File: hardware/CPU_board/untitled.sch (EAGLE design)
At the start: 67 parts, among them IC1 MAX232ECWE, IC2 MAX232ECWE, IC3 AM29F040J, IC4 74HCT138D, IC5 LM2596S, IC6 74245SSOP, IC7 74245SSOP, IC8 74245SSOP, J2 POWER_JACKSLT, U1 AS6C4008-55SIN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

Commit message: Power trace updated
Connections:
- net 5V: now also IC7P.VCC, IC8P.VCC
- net GND: now also IC7P.GND, IC8A.A1, IC8A.A2, IC8A.A3, IC8A.A4, IC8A.G, IC8P.GND
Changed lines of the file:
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@@
 <part name="IC8" library="74xx-eu" deviceset="74*245" device="SSOP" value="74245SSOP"/>
 <part name="GND23" library="supply1" deviceset="GND" device=""/>
+<part name="GND25" library="supply1" deviceset="GND" device=""/>
 </parts>
 <sheets>
@@
 <instance part="IC8" gate="A" x="381" y="228.6"/>
 <instance part="GND23" gate="1" x="396.24" y="254"/>
+<instance part="GND25" gate="1" x="365.76" y="210.82"/>
+<instance part="IC7" gate="P" x="25.4" y="190.5"/>
+<instance part="IC8" gate="P" x="35.56" y="190.5"/>
 </instances>
 <busses>
@@
 <wire x1="15.24" y1="180.34" x2="15.24" y2="182.88" width="0.1524" layer="91"/>
 <junction x="5.08" y="180.34"/>
+<pinref part="IC7" gate="P" pin="GND"/>
+<wire x1="15.24" y1="180.34" x2="25.4" y2="180.34" width="0.1524" layer="91"/>
+<wire x1="25.4" y1="180.34" x2="25.4" y2="182.88" width="0.1524" layer="91"/>
+<junction x="15.24" y="180.34"/>
+<pinref part="IC8" gate="P" pin="GND"/>
+<wire x1="25.4" y1="180.34" x2="35.56" y2="180.34" width="0.1524" layer="91"/>
+<wire x1="35.56" y1="180.34" x2="35.56" y2="182.88" width="0.1524" layer="91"/>
+<junction x="25.4" y="180.34"/>
 </segment>
 <segment>
@@
 <junction x="396.24" y="281.94"/>
 </segment>
+<segment>
+<pinref part="IC8" gate="A" pin="G"/>
+<pinref part="GND25" gate="1" pin="GND"/>
+<wire x1="368.3" y1="215.9" x2="365.76" y2="215.9" width="0.1524" layer="91"/>
+<wire x1="365.76" y1="215.9" x2="365.76" y2="213.36" width="0.1524" layer="91"/>
+<pinref part="IC8" gate="A" pin="A1"/>
+<wire x1="368.3" y1="241.3" x2="365.76" y2="241.3" width="0.1524" layer="91"/>
+<wire x1="365.76" y1="241.3" x2="365.76" y2="238.76" width="0.1524" layer="91"/>
+<junction x="365.76" y="215.9"/>
+<pinref part="IC8" gate="A" pin="A2"/>
+<wire x1="365.76" y1="238.76" x2="365.76" y2="236.22" width="0.1524" layer="91"/>
+<wire x1="365.76" y1="236.22" x2="365.76" y2="233.68" width="0.1524" layer="91"/>
+<wire x1="365.76" y1="233.68" x2="365.76" y2="215.9" width="0.1524" layer="91"/>
+<wire x1="368.3" y1="238.76" x2="365.76" y2="238.76" width="0.1524" layer="91"/>
+<junction x="365.76" y="238.76"/>
+<pinref part="IC8" gate="A" pin="A3"/>
+<wire x1="368.3" y1="236.22" x2="365.76" y2="236.22" width="0.1524" layer="91"/>
+<junction x="365.76" y="236.22"/>
+<pinref part="IC8" gate="A" pin="A4"/>
+<wire x1="368.3" y1="233.68" x2="365.76" y2="233.68" width="0.1524" layer="91"/>
+<junction x="365.76" y="233.68"/>
+</segment>
 </net>
 <net name="5V" class="0">
@@
 <wire x1="15.24" y1="200.66" x2="15.24" y2="198.12" width="0.1524" layer="91"/>
 <junction x="5.08" y="200.66"/>
-</segment>
-<segment>
+<pinref part="IC7" gate="P" pin="VCC"/>
+<wire x1="15.24" y1="200.66" x2="25.4" y2="200.66" width="0.1524" layer="91"/>
+<wire x1="25.4" y1="200.66" x2="25.4" y2="198.12" width="0.1524" layer="91"/>
+<junction x="15.24" y="200.66"/>
+<pinref part="IC8" gate="P" pin="VCC"/>
+<wire x1="25.4" y1="200.66" x2="35.56" y2="200.66" width="0.1524" layer="91"/>
+<wire x1="35.56" y1="200.66" x2="35.56" y2="198.12" width="0.1524" layer="91"/>
+<junction x="25.4" y="200.66"/>
+</segment>
+<segment>

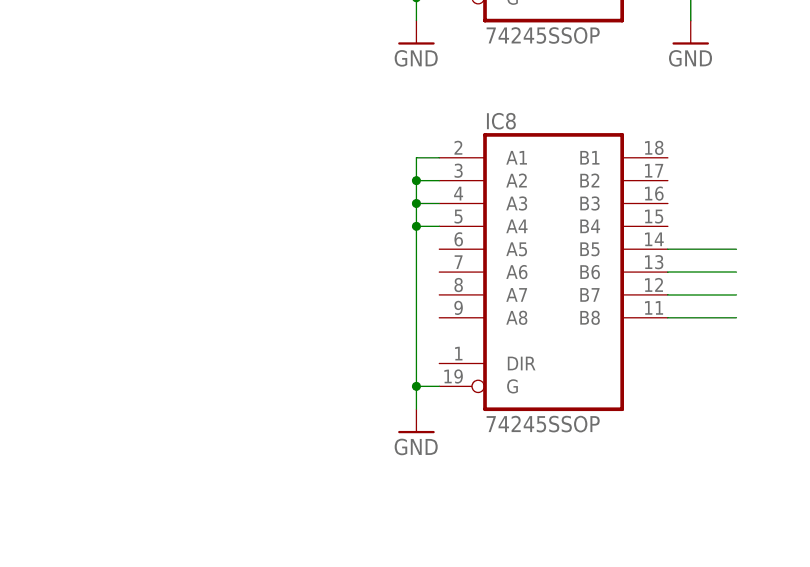
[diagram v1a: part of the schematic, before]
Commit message: Printer port wired
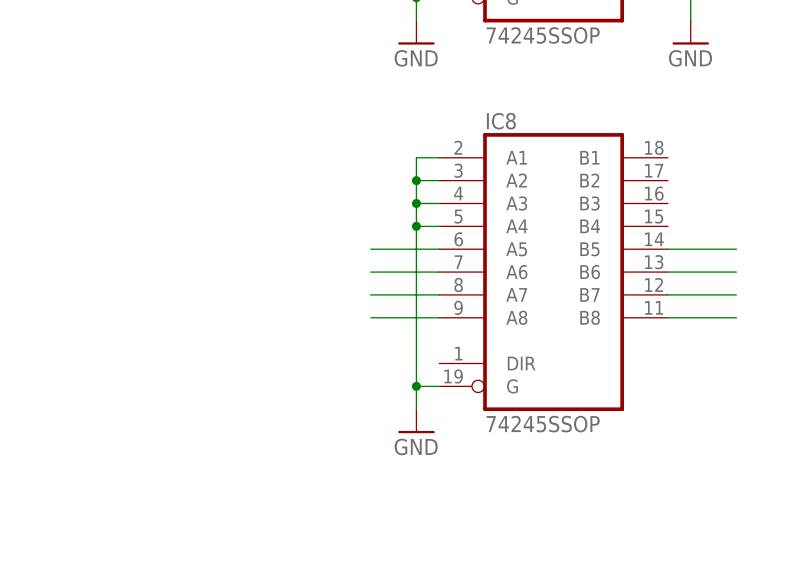
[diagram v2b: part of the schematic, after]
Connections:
- net /ACK: now also IC8A.A8
- net BUSY: now also IC8A.A7
- net PE: now also IC8A.A6
- net SLCT: now also IC8A.A5
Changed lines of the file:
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@@
 <label x="441.96" y="266.7" size="1.4224" layer="95" rot="R180" xref="yes"/>
+</segment>
+<segment>
+<pinref part="IC8" gate="A" pin="A8"/>
+<wire x1="368.3" y1="223.52" x2="360.68" y2="223.52" width="0.1524" layer="91"/>
 </segment>
 </net>
@@
 <label x="441.96" y="264.16" size="1.4224" layer="95" rot="R180" xref="yes"/>
 </segment>
+<segment>
+<pinref part="IC8" gate="A" pin="A7"/>
+<wire x1="368.3" y1="226.06" x2="360.68" y2="226.06" width="0.1524" layer="91"/>
+</segment>
 </net>
 <net name="PE" class="0">
@@
 <wire x1="452.12" y1="261.62" x2="441.96" y2="261.62" width="0.1524" layer="91"/>
 <label x="441.96" y="261.62" size="1.4224" layer="95" rot="R180" xref="yes"/>
+</segment>
+<segment>
+<pinref part="IC8" gate="A" pin="A6"/>
+<wire x1="368.3" y1="228.6" x2="360.68" y2="228.6" width="0.1524" layer="91"/>
 </segment>
 </net>
@@
 <label x="441.96" y="259.08" size="1.4224" layer="95" rot="R180" xref="yes"/>
 </segment>
+<segment>
+<pinref part="IC8" gate="A" pin="A5"/>
+<wire x1="368.3" y1="231.14" x2="360.68" y2="231.14" width="0.1524" layer="91"/>
+</segment>
 </net>

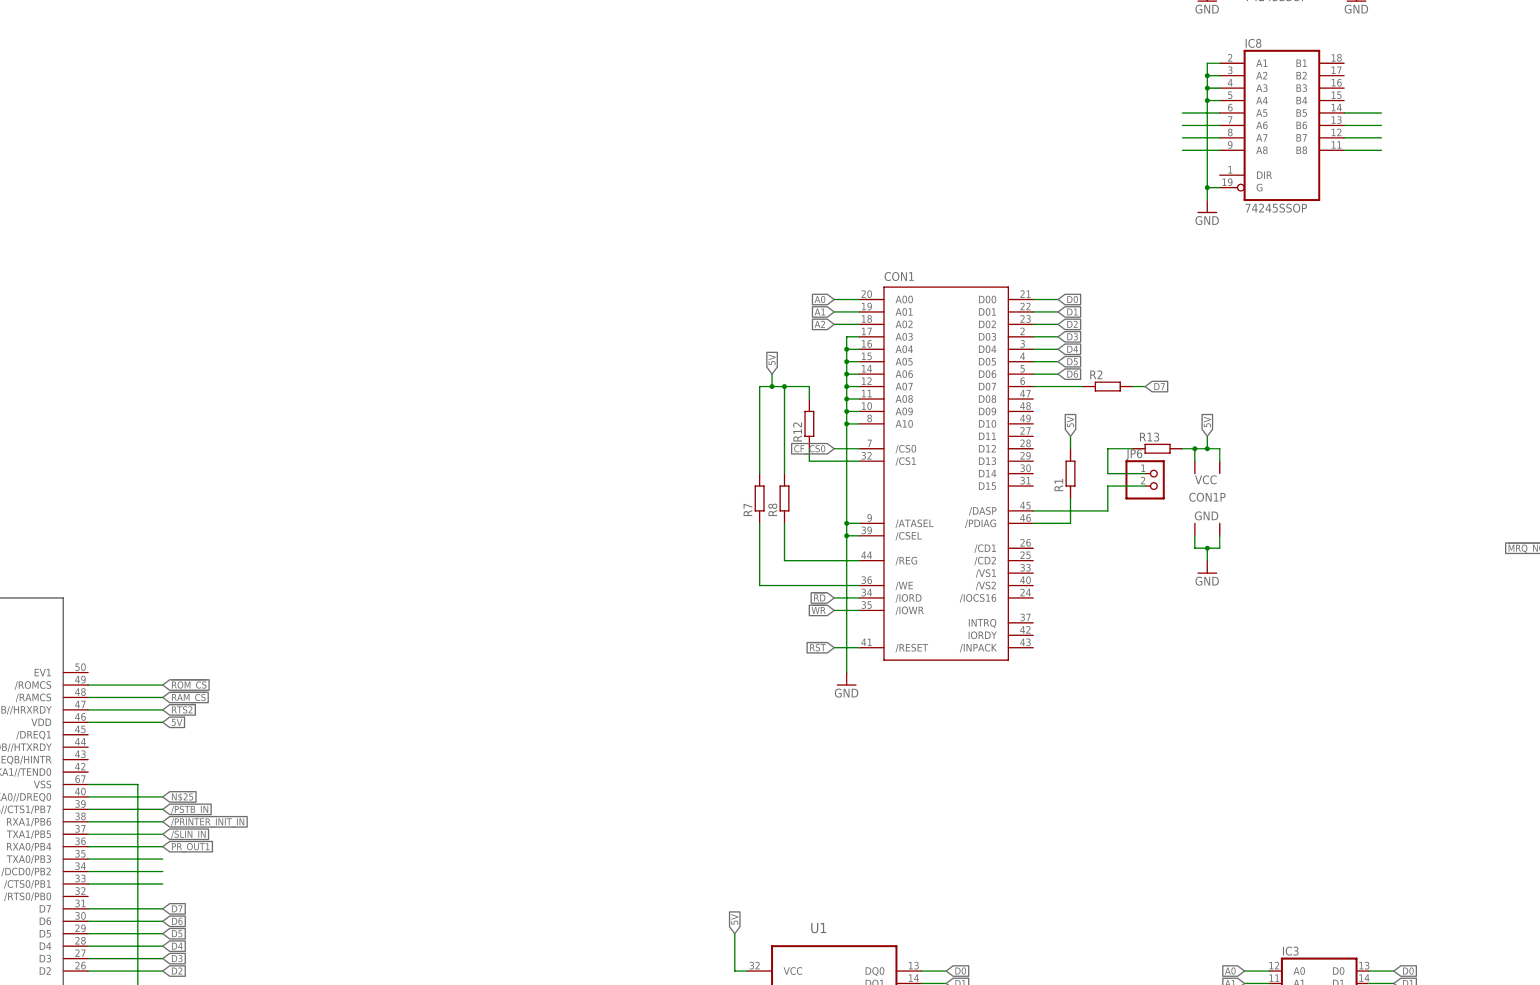
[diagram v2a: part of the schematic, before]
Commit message: Printer error line routed
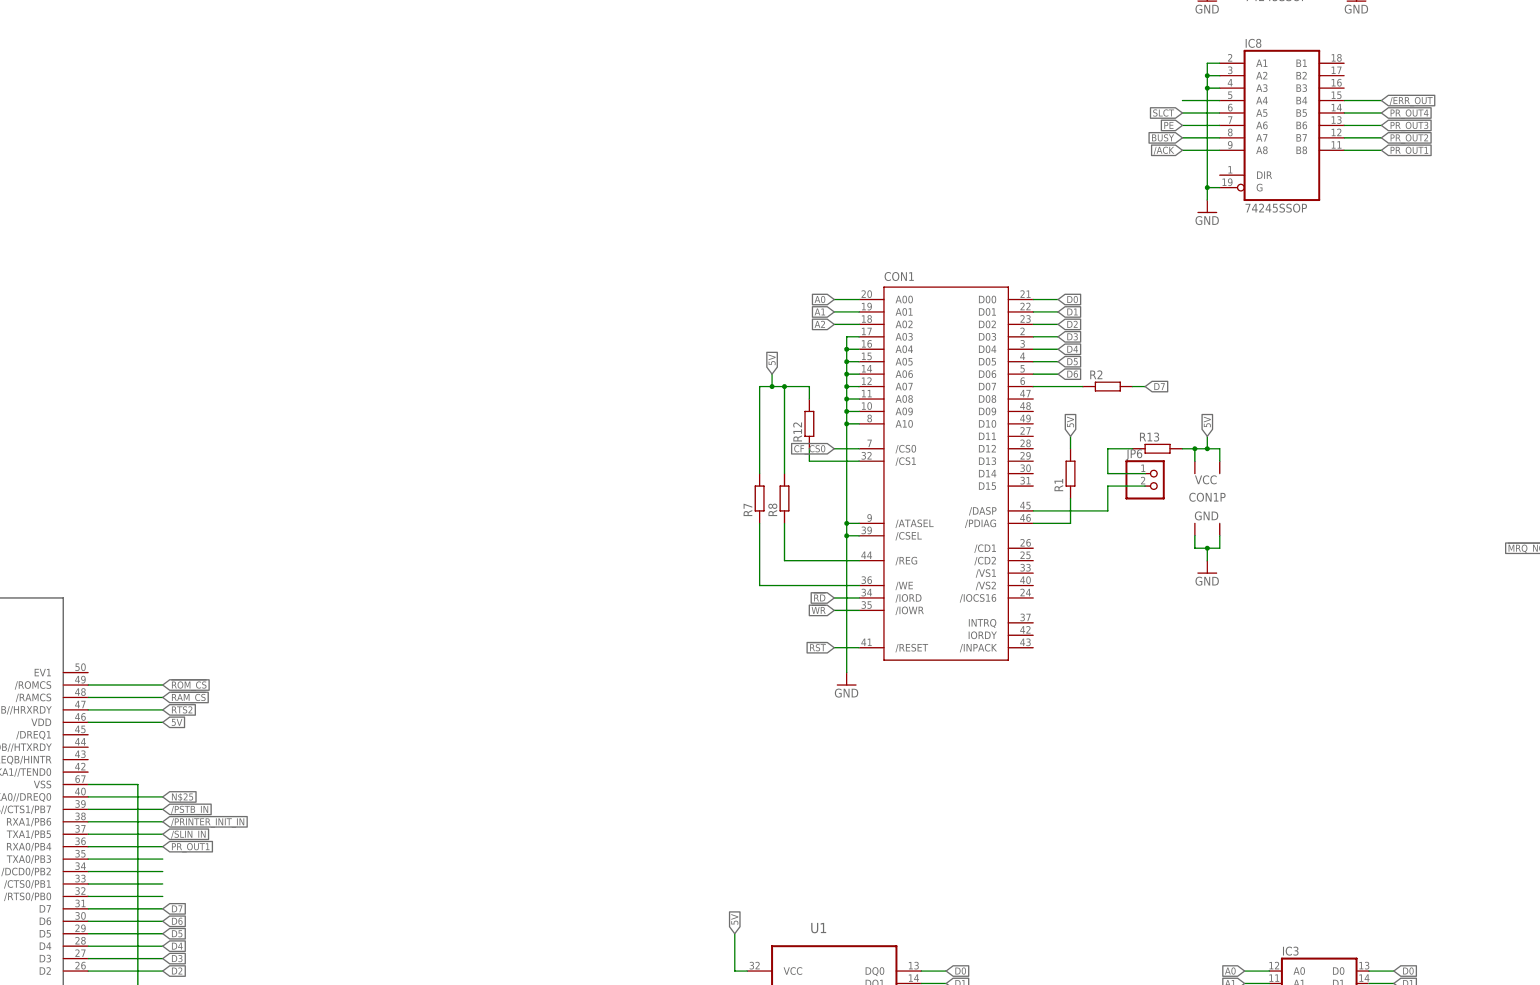
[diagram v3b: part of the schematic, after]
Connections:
- new net /ERR_OUT: IC8A.B4, U$1./RTS0/PB0
- net /ERR: now also IC8A.A4
- net GND: no longer IC8A.A4
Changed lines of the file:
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@@
 <pinref part="IC8" gate="A" pin="A2"/>
 <wire x1="365.76" y1="238.76" x2="365.76" y2="236.22" width="0.1524" layer="91"/>
-<wire x1="365.76" y1="236.22" x2="365.76" y2="233.68" width="0.1524" layer="91"/>
-<wire x1="365.76" y1="233.68" x2="365.76" y2="215.9" width="0.1524" layer="91"/>
+<wire x1="365.76" y1="236.22" x2="365.76" y2="215.9" width="0.1524" layer="91"/>
 <wire x1="368.3" y1="238.76" x2="365.76" y2="238.76" width="0.1524" layer="91"/>
 <junction x="365.76" y="238.76"/>
@@
 <wire x1="368.3" y1="236.22" x2="365.76" y2="236.22" width="0.1524" layer="91"/>
 <junction x="365.76" y="236.22"/>
-<pinref part="IC8" gate="A" pin="A4"/>
-<wire x1="368.3" y1="233.68" x2="365.76" y2="233.68" width="0.1524" layer="91"/>
-<junction x="365.76" y="233.68"/>
 </segment>
 </net>
@@
 <label x="469.9" y="287.02" size="1.4224" layer="95" xref="yes"/>
 </segment>
+<segment>
+<pinref part="IC8" gate="A" pin="A4"/>
+<wire x1="368.3" y1="233.68" x2="360.68" y2="233.68" width="0.1524" layer="91"/>
+</segment>
 </net>
 <net name="/AFD" class="0">
@@
 <pinref part="IC8" gate="A" pin="A8"/>
 <wire x1="368.3" y1="223.52" x2="360.68" y2="223.52" width="0.1524" layer="91"/>
+<label x="360.68" y="223.52" size="1.4224" layer="95" rot="R180" xref="yes"/>
 </segment>
 </net>
@@
 <pinref part="IC8" gate="A" pin="A7"/>
 <wire x1="368.3" y1="226.06" x2="360.68" y2="226.06" width="0.1524" layer="91"/>
+<label x="360.68" y="226.06" size="1.4224" layer="95" rot="R180" xref="yes"/>
 </segment>
 </net>
@@
 <pinref part="IC8" gate="A" pin="A6"/>
 <wire x1="368.3" y1="228.6" x2="360.68" y2="228.6" width="0.1524" layer="91"/>
+<label x="360.68" y="228.6" size="1.4224" layer="95" rot="R180" xref="yes"/>
 </segment>
 </net>
@@
 <pinref part="IC8" gate="A" pin="A5"/>
 <wire x1="368.3" y1="231.14" x2="360.68" y2="231.14" width="0.1524" layer="91"/>
+<label x="360.68" y="231.14" size="1.4224" layer="95" rot="R180" xref="yes"/>
 </segment>
 </net>
@@
 <pinref part="IC8" gate="A" pin="B8"/>
 <wire x1="393.7" y1="223.52" x2="401.32" y2="223.52" width="0.1524" layer="91"/>
+<label x="401.32" y="223.52" size="1.4224" layer="95" xref="yes"/>
 </segment>
 </net>
@@
 <pinref part="IC8" gate="A" pin="B7"/>
 <wire x1="393.7" y1="226.06" x2="401.32" y2="226.06" width="0.1524" layer="91"/>
+<label x="401.32" y="226.06" size="1.4224" layer="95" xref="yes"/>
 </segment>
 <segment>
@@
 <pinref part="IC8" gate="A" pin="B6"/>
 <wire x1="393.7" y1="228.6" x2="401.32" y2="228.6" width="0.1524" layer="91"/>
+<label x="401.32" y="228.6" size="1.4224" layer="95" xref="yes"/>
 </segment>
 </net>
@@
 <pinref part="IC8" gate="A" pin="B5"/>
 <wire x1="393.7" y1="231.14" x2="401.32" y2="231.14" width="0.1524" layer="91"/>
+<label x="401.32" y="231.14" size="1.4224" layer="95" xref="yes"/>
 </segment>
 <segment>
@@
 </segment>
 </net>
+<net name="/ERR_OUT" class="0">
+<segment>
+<wire x1="393.7" y1="233.68" x2="401.32" y2="233.68" width="0.1524" layer="91"/>
+<pinref part="IC8" gate="A" pin="B4"/>
+<label x="401.32" y="233.68" size="1.4224" layer="95" xref="yes"/>
+</segment>
+<segment>
+<pinref part="U$1" gate="G$1" pin="/RTS0/PB0"/>
+<wire x1="137.16" y1="71.12" x2="152.4" y2="71.12" width="0.1524" layer="91"/>
+</segment>
+</net>

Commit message: Capacitors added
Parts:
- added C24: (no value), rcl:C-EUC0603
- added C26, C27: (no value), rcl:C-EUC0402
- added R11: (no value), rcl:R-EU_R0603
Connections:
- new net N$26: IC8A.DIR, R11.1
- net 5V: now also C24.1, C26.1, C27.1, R11.2
- net GND: now also C24.2, C26.2, C27.2
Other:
- moved on the sheet: C1, C11, C12, C13, C14, C17, C2, C3

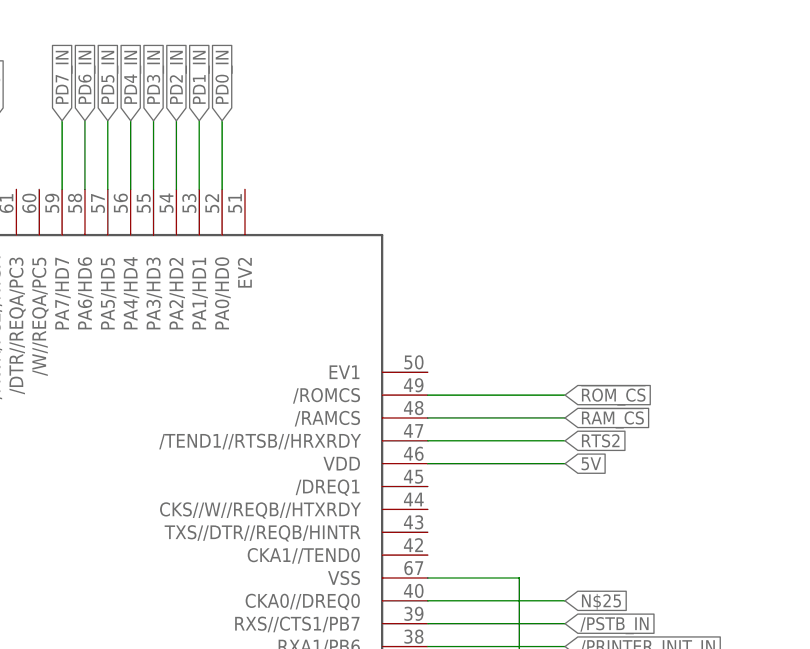
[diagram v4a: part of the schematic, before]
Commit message: Dangling signals fixed
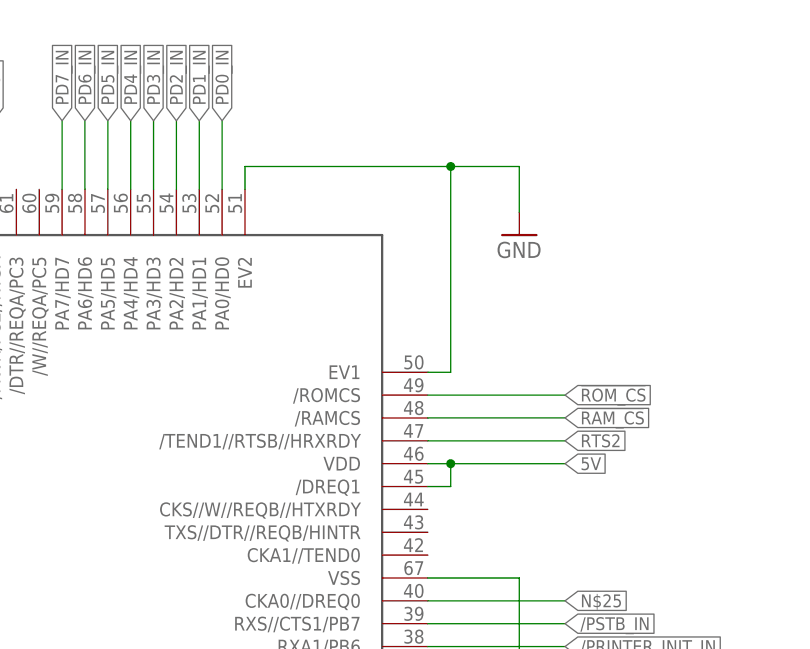
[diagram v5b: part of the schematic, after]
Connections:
- net 5V: now also U$1./DREQ1
- net GND: now also U$1.EV1, U$1.EV2
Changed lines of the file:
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@@
 <part name="C26" library="rcl" deviceset="C-EU" device="C0402"/>
 <part name="C27" library="rcl" deviceset="C-EU" device="C0402"/>
+<part name="GND26" library="supply1" deviceset="GND" device=""/>
 </parts>
 <sheets>
@@
 <instance part="C26" gate="G$1" x="-50.8" y="190.5"/>
 <instance part="C27" gate="G$1" x="-43.18" y="190.5"/>
+<instance part="GND26" gate="1" x="147.32" y="132.08"/>
 </instances>
 <busses>
@@
 <junction x="365.76" y="236.22"/>
 </segment>
+<segment>
+<pinref part="U$1" gate="G$1" pin="EV2"/>
+<wire x1="116.84" y1="137.16" x2="116.84" y2="139.7" width="0.1524" layer="91"/>
+<wire x1="116.84" y1="139.7" x2="139.7" y2="139.7" width="0.1524" layer="91"/>
+<wire x1="139.7" y1="139.7" x2="139.7" y2="116.84" width="0.1524" layer="91"/>
+<pinref part="U$1" gate="G$1" pin="EV1"/>
+<wire x1="139.7" y1="116.84" x2="137.16" y2="116.84" width="0.1524" layer="91"/>
+<wire x1="139.7" y1="139.7" x2="147.32" y2="139.7" width="0.1524" layer="91"/>
+<wire x1="147.32" y1="139.7" x2="147.32" y2="134.62" width="0.1524" layer="91"/>
+<junction x="139.7" y="139.7"/>
+<pinref part="GND26" gate="1" pin="GND"/>
+</segment>
 </net>
 <net name="5V" class="0">
@@
 <segment>
 <pinref part="U$1" gate="G$1" pin="VDD@2"/>
-<wire x1="137.16" y1="106.68" x2="152.4" y2="106.68" width="0.1524" layer="91"/>
+<wire x1="137.16" y1="106.68" x2="139.7" y2="106.68" width="0.1524" layer="91"/>
 <label x="152.4" y="106.68" size="1.4224" layer="95" xref="yes"/>
-</segment>
-<segment>
+<pinref part="U$1" gate="G$1" pin="/DREQ1"/>
+<wire x1="139.7" y1="106.68" x2="152.4" y2="106.68" width="0.1524" layer="91"/>
+<wire x1="137.16" y1="104.14" x2="139.7" y2="104.14" width="0.1524" layer="91"/>
+<wire x1="139.7" y1="104.14" x2="139.7" y2="106.68" width="0.1524" layer="91"/>
+<junction x="139.7" y="106.68"/>
+</segment>
+<segment>
